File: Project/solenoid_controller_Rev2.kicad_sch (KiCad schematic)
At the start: 110 parts, among them J1 Conn_01x04_Pin, J10 Conn_01x02_Socket, J11 Conn_01x02_Socket, J12 Conn_01x02_Socket, J13 Conn_01x02_Socket, J14 Conn_01x02_Socket, J15 Conn_01x02_Socket, J16 Conn_01x02_Socket, J17 Conn_01x02_Socket, J18 Conn_01x02_Socket, J19 Conn_01x02_Socket, J2 Conn_01x06_Socket, J20 Conn_01x02_Socket, J21 Conn_02x05_Odd_Even, J22 Conn_01x04_Pin, J3 Conn_01x06_Socket, J4 Conn_01x02_Socket, J5 Conn_01x02_Socket, J6 Conn_01x02_Socket, J7 Conn_01x02_Socket, J8 Conn_01x02_Socket, J9 Conn_01x02_Socket, SW1 SW_MEC_5E, U1 SSM6N7002KFU, U2 FT231XS-R, U3 THVD2442, U4 NCP1117-3.3_SOT223, U5 SSM6N7002KFU, U6 DAC60502, U7 NCV272DMR2G, U8 NCV272DMR2G, Y1 24 MHz

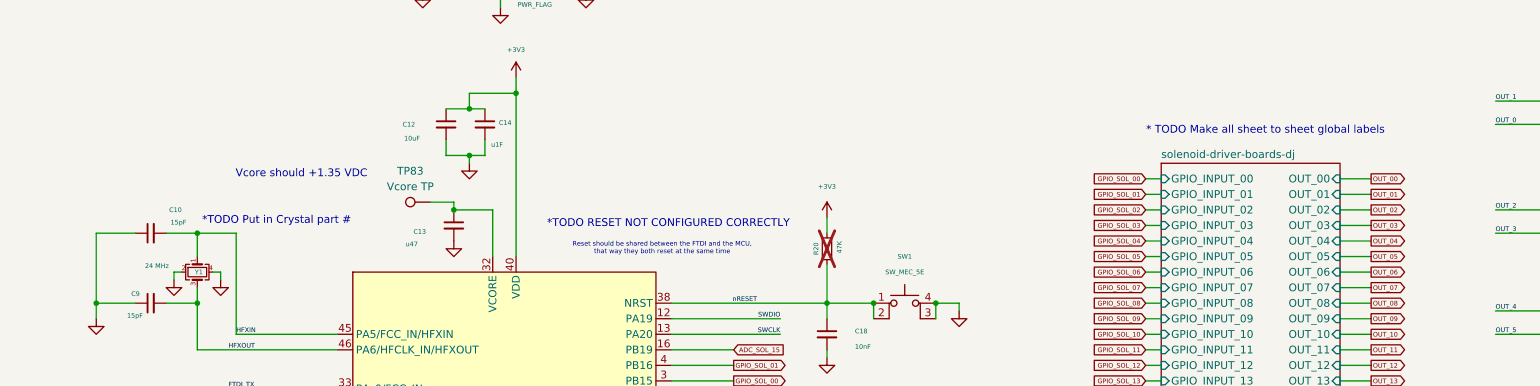
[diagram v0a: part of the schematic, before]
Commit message: FINISHED TODO LIST and updated current sense
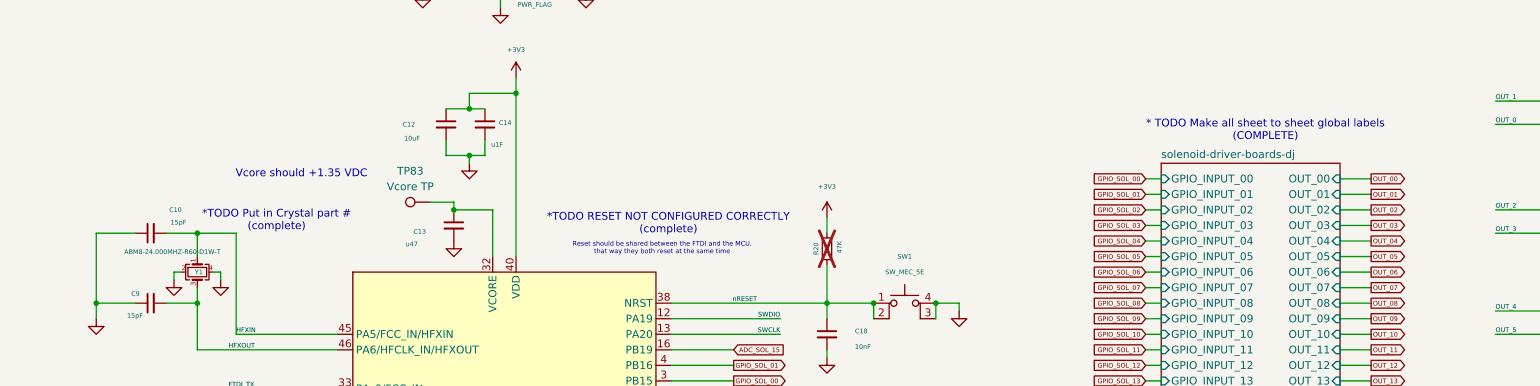
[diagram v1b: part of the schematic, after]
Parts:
- Y1: value 24 MHz -> ABM8-24.000MHZ-R60-D1W-T
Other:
- note added: "* TODO Make all sheet to sheet global labels (COMPLETE)"
- note added: "*TODO Put in Crystal part # (complete)"
- note added: "*TODO RESET NOT CONFIGURED CORRECTLY (complete)"
- note removed: "* TODO Make all sheet to sheet global labels"
- note removed: "*TODO Put in Crystal part #"
- note removed: "*TODO RESET NOT CONFIGURED CORRECTLY"
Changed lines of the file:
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@@
 		)
 	)
-	(text "* TODO Make all sheet to sheet global labels"
+	(text "* TODO Make all sheet to sheet global labels\n(COMPLETE)"
 		(exclude_from_sim no)
 		(at 297.688 70.866 0)
@@
 		)
 	)
-	(text "*TODO Put in Crystal part #"
+	(text "*TODO Put in Crystal part #\n(complete)"
 		(exclude_from_sim no)
 		(at 136.144 85.598 0)
@@
 		)
 	)
-	(text "*TODO RESET NOT CONFIGURED CORRECTLY"
+	(text "*TODO RESET NOT CONFIGURED CORRECTLY\n(complete)"
 		(exclude_from_sim no)
 		(at 200.152 86.106 0)
@@
 			)
 		)
-		(property "Value" "24 MHz"
-			(at 116.586 92.964 90)
+		(property "Value" "ABM8-24.000MHZ-R60-D1W-T"
+			(at 119.126 90.678 90)
 			(effects
 				(font
